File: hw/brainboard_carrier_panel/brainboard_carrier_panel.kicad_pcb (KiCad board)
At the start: 2 copper layers, 40.3 x 128.5 mm, 26 parts, among them J1 3.5mm, J10 3.5mm, J12 3.5mm, J2 3.5mm, J3 3.5mm, J4 3.5mm, J5 3.5mm, J6 3.5mm, J7 3.5mm, J8 3.5mm, J9 3.5mm, SW1 SW_Push, SW2 SW_Push

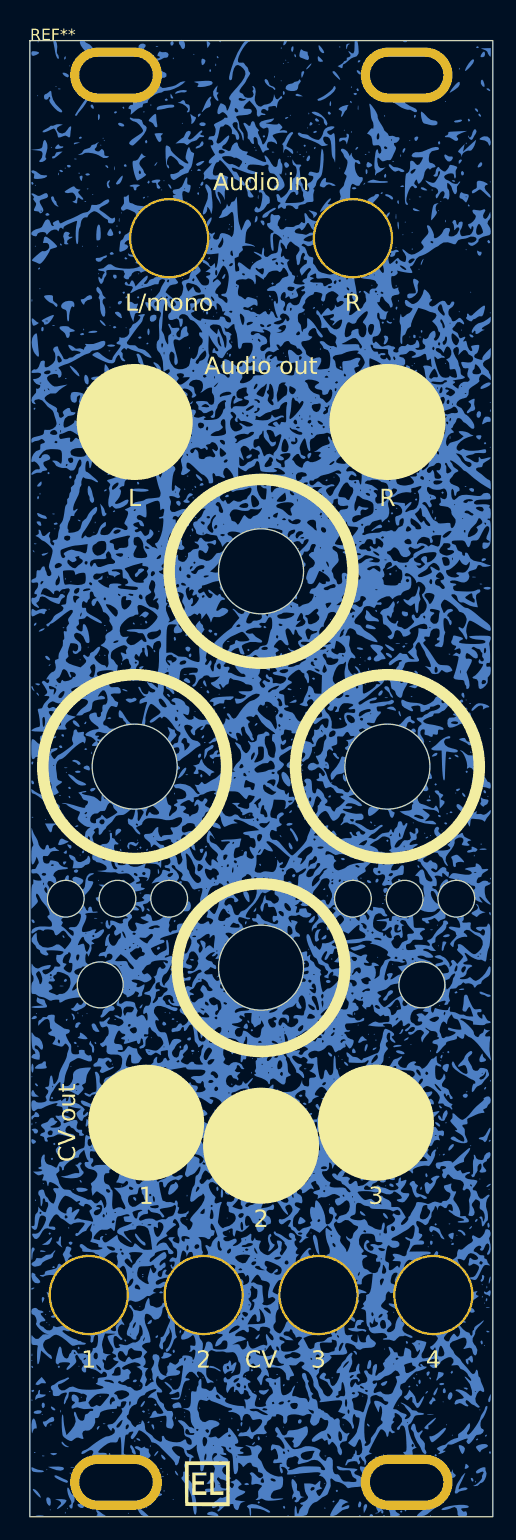
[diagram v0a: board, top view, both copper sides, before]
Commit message: More tiny adjustments. As ordered from JLCPCB.
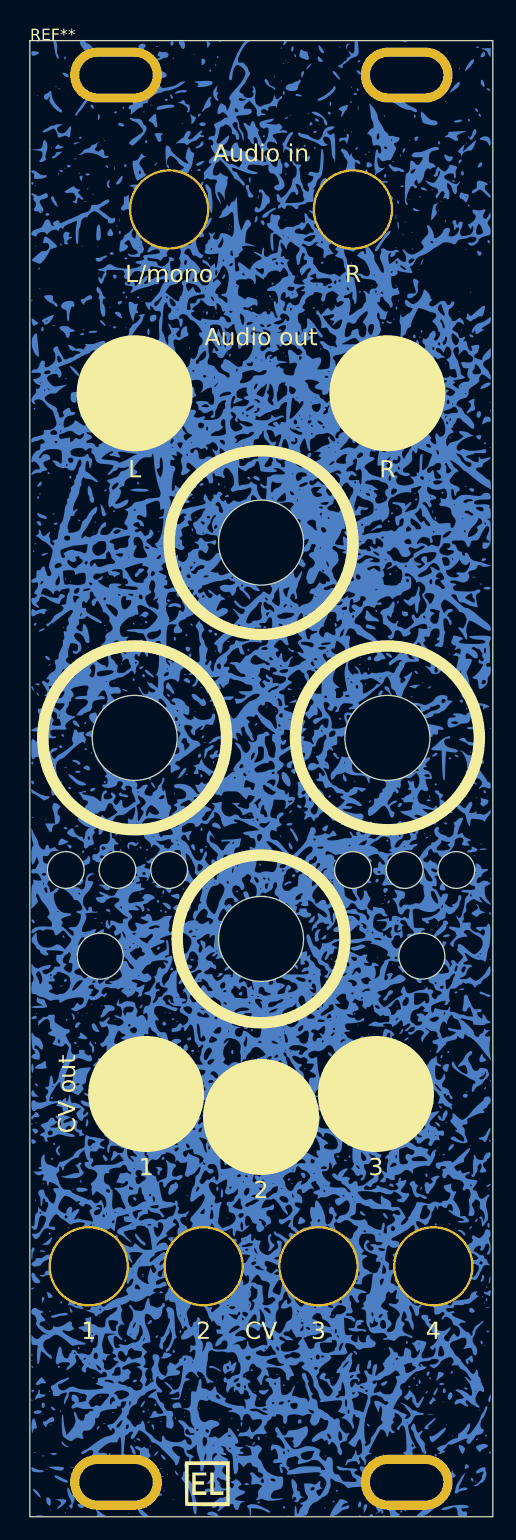
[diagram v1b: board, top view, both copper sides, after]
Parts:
- moved D1 2.50 mm to (103.0, 110.0)
- moved D2 2.50 mm to (107.5, 110.0)
- moved D3 2.50 mm to (112.0, 110.0)
- moved D4 2.50 mm to (128.0, 110.0)
- moved D5 2.50 mm to (132.5, 110.0)
- moved D6 2.50 mm to (137.0, 110.0)
- moved J1 2.50 mm to (105.0, 144.5)
- moved J10 2.50 mm to (120.0, 131.5)
- moved J12 2.50 mm to (130.0, 129.5)
- moved J2 2.50 mm to (115.0, 144.5)
- moved J3 2.50 mm to (125.0, 144.5)
- moved J4 2.50 mm to (135.0, 144.5)
- moved J5 2.50 mm to (112.0, 52.5)
- moved J6 2.50 mm to (128.0, 52.5)
- moved J7 2.50 mm to (109.0, 68.5)
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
